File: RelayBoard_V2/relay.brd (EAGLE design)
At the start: 127 x 114.3 mm, 30 parts, among them K1 T9AS1D12-5, K2 T9AS1D12-5, T1 2N2222, T2 2N2222, T3 2N2222, T4 2N2222, X1 22-23-2021

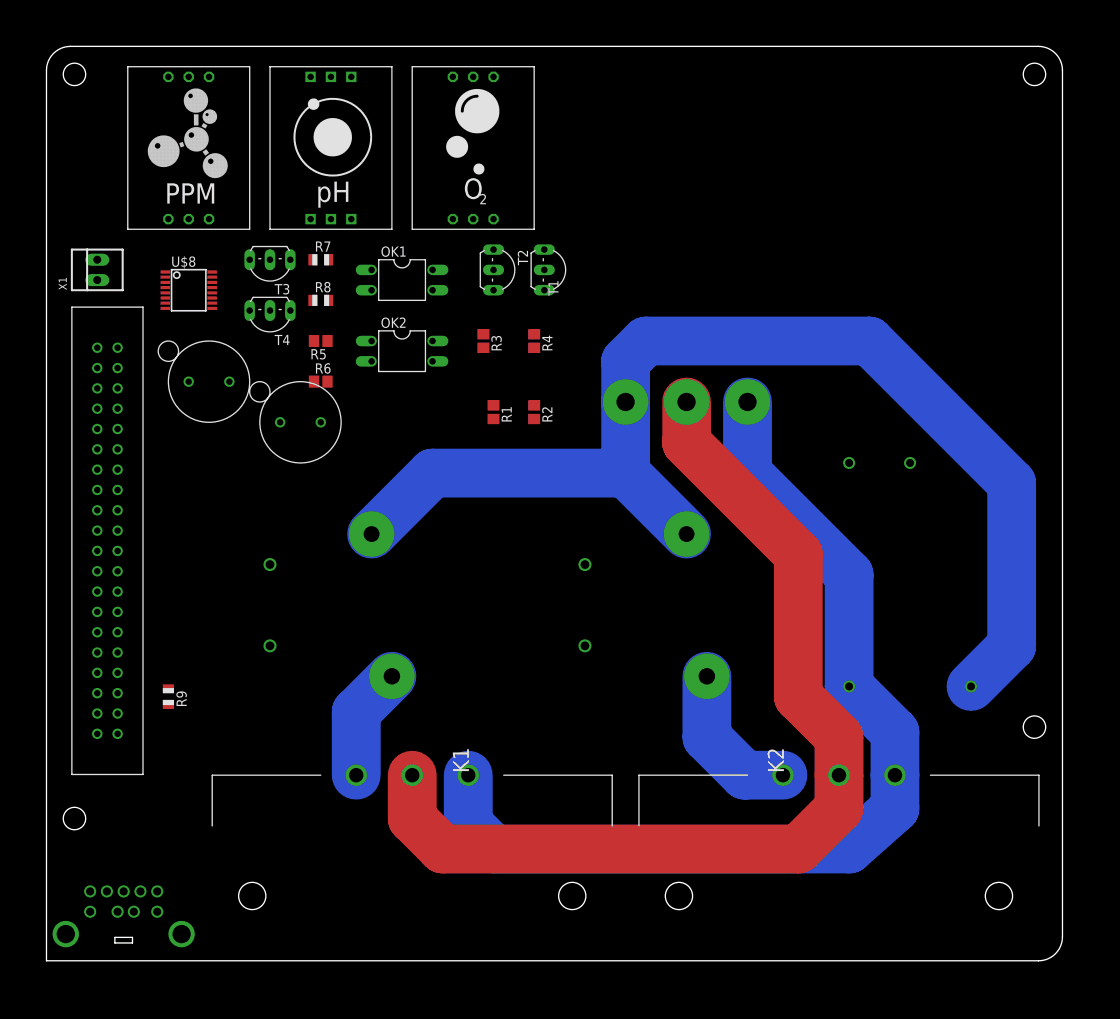
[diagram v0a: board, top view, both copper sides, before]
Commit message: Route everything. Add logo
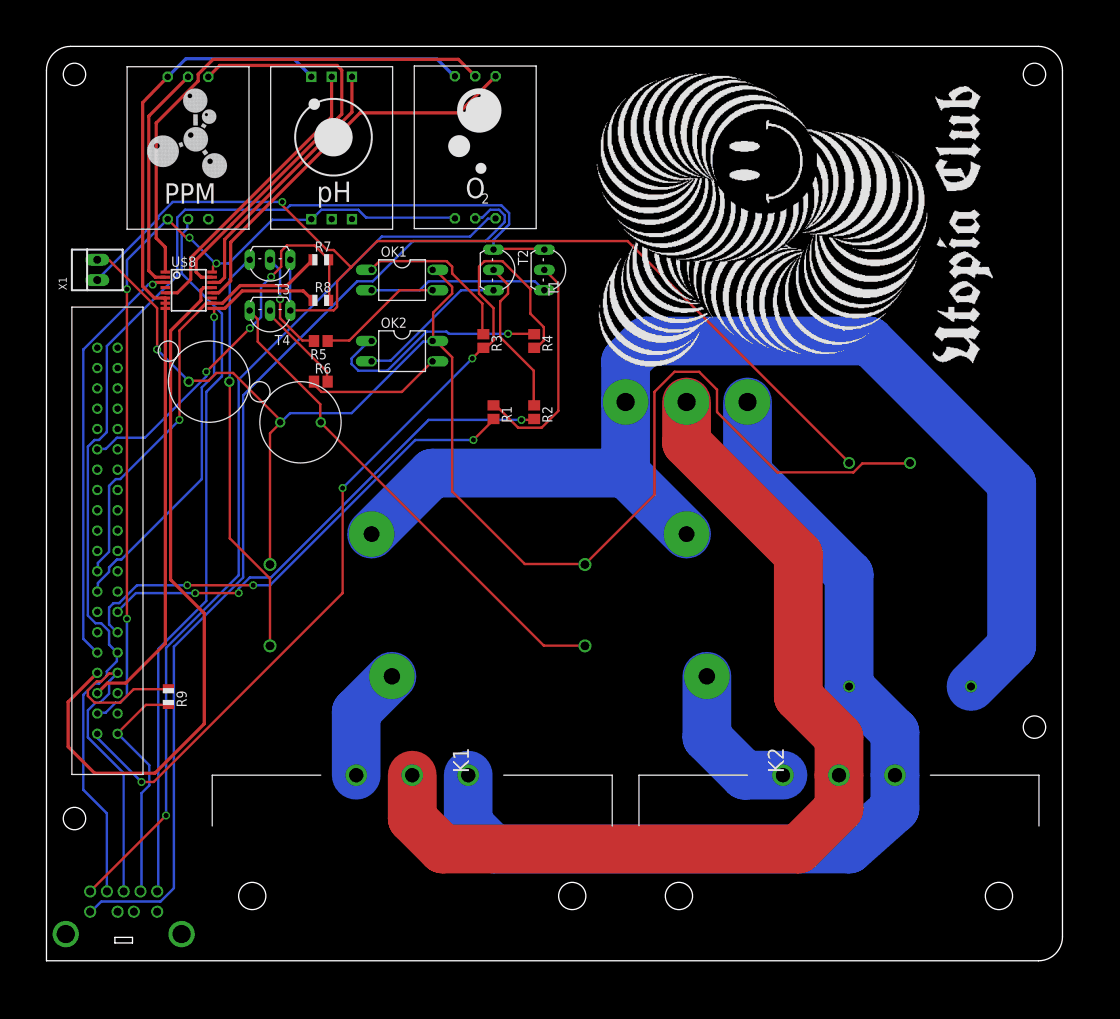
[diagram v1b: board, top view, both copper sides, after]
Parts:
- moved U$9 0.27 mm to (53.6, 101.7)
- moved U$10 0.08 mm to (35.6, 101.6)
- moved U$11 0.08 mm to (17.7, 101.6)
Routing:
- net N$32: track 0.00 -> 194.2 mm, vias 0 -> 1
- net DGND: track 0.00 -> 148.9 mm
- net AGND: track 0.00 -> 132.8 mm, vias 0 -> 1
- net N$30: track 0.00 -> 126.5 mm
- net N$41: track 0.00 -> 123.8 mm
- net N$31: track 0.00 -> 112.1 mm, vias 0 -> 1
- net N$6: track 0.00 -> 109.8 mm, vias 0 -> 3
- net N$33: track 0.00 -> 109.1 mm, vias 0 -> 4
- net N$7: track 0.00 -> 90.7 mm
- net N$37: track 0.00 -> 89.8 mm
- net N$26: track 0.00 -> 63.6 mm
- net N$1: track 0.00 -> 62.4 mm, vias 0 -> 3
- net N$16: track 0.00 -> 62.3 mm
- net N$2: track 0.00 -> 61.5 mm, vias 0 -> 3
- net N$28: track 0.00 -> 55.9 mm, vias 0 -> 1
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
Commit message: GND pour and add gerbers
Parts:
- renumbered U$8 to MUX
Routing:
- added copper zone on layer 1, net GND
- added copper zone on layer 16, net GND
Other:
- board text added: "jackbowen.github.io"

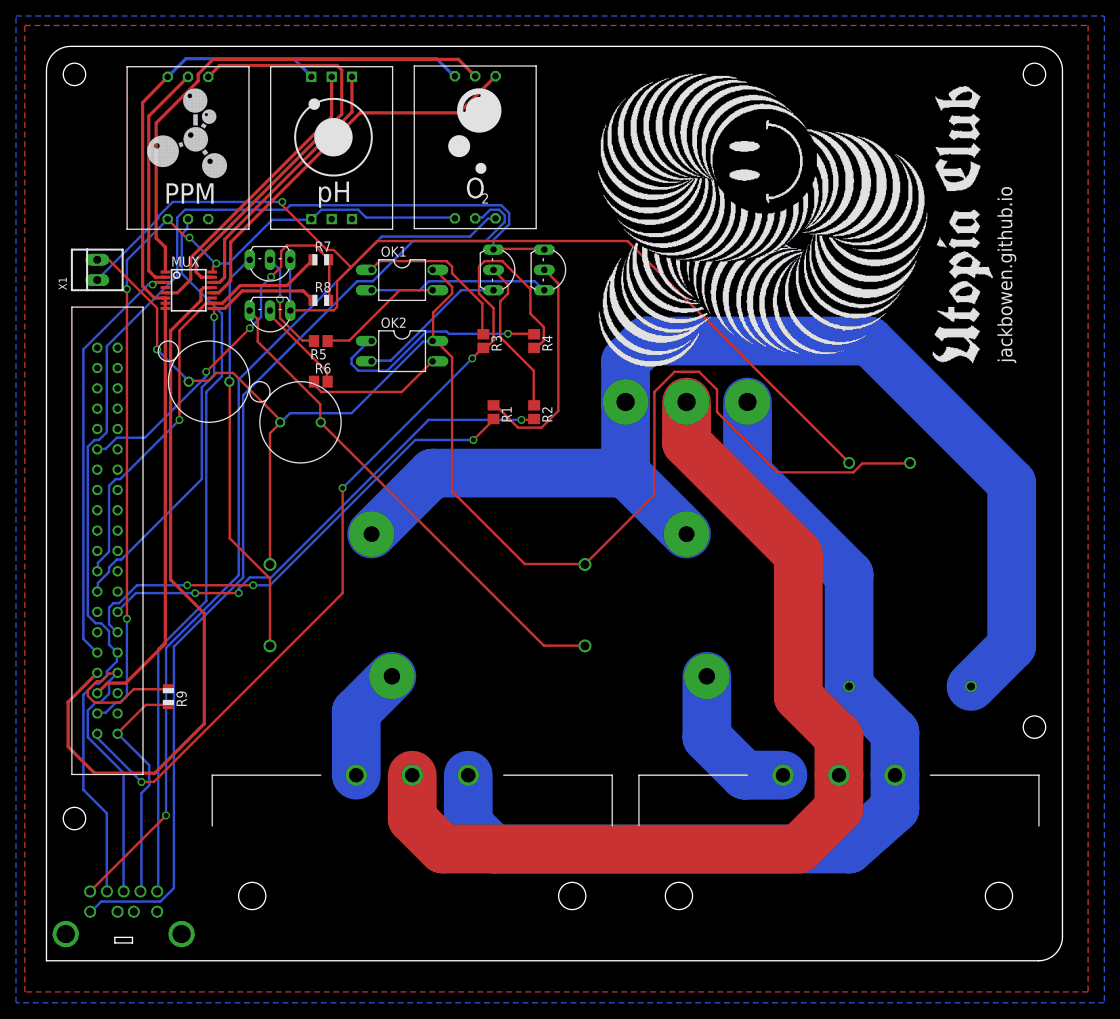
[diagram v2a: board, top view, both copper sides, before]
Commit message: Reduced DPI of silkscreen to OSH Park can actually fabricate them. New gerbers.
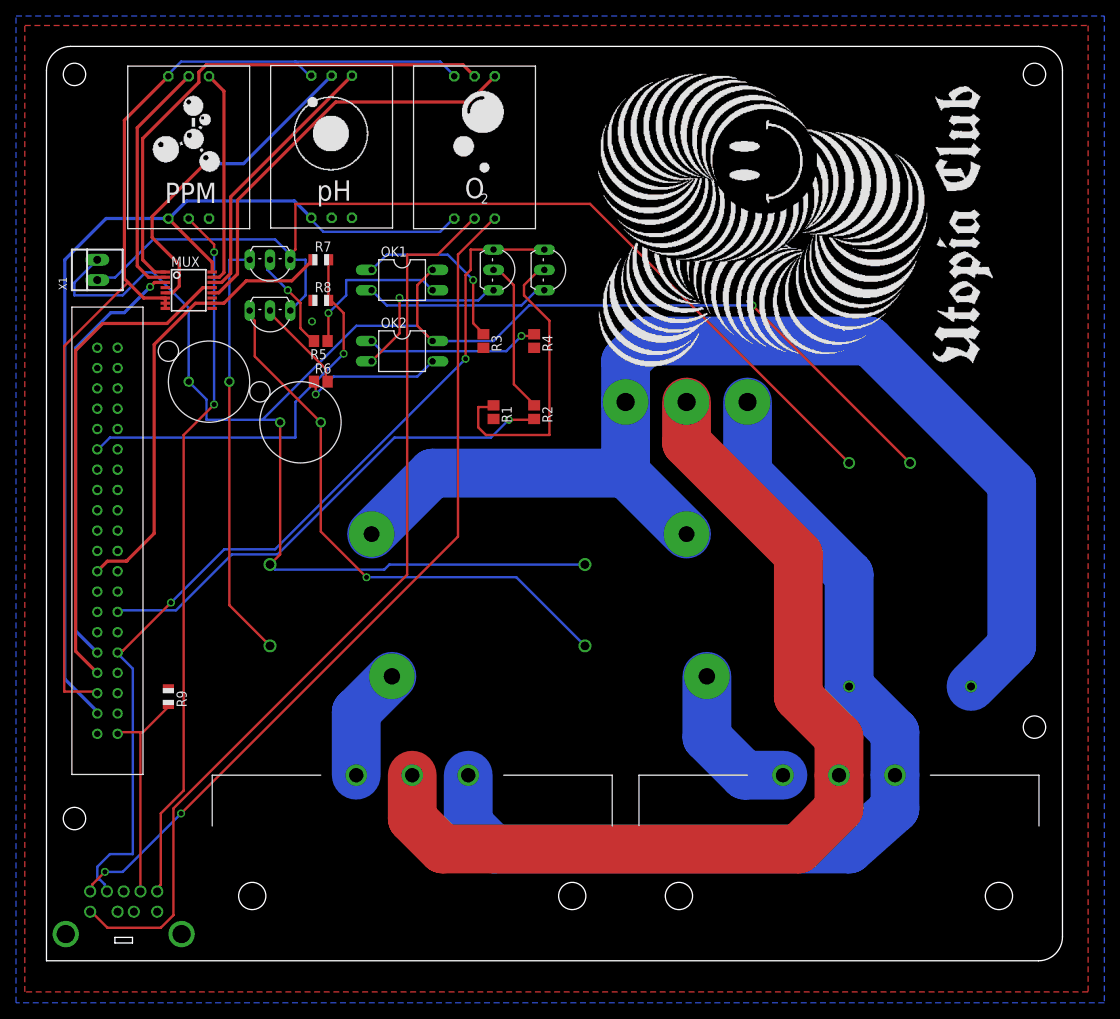
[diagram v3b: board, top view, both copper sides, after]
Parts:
- removed U$10: ATLAS_PH_WITH_ICON, BloomWall:ATLAS_PH_WITH_ICON
- removed U$11: ATLAS_PPM_WITH_ICON, BloomWall:ATLAS_PPM_WITH_ICON
- added U$5: ATLAS_DO_WITH_ICON, BloomWall:ATLAS_DO_WITH_ICON
- added U$8: ATLAS_PH_WITH_ICON, BloomWall:ATLAS_PH_WITH_ICON
- U$9: value ATLAS_DO_WITH_ICON -> ATLAS_PPM_WITH_ICON; device BloomWall:ATLAS_DO_WITH_ICON -> BloomWall:ATLAS_PPM_WITH_ICON
- moved U$9 35.8 mm to (17.8, 101.7)
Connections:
- removed net GND2: U$1.GND2
- removed net GND3: U$1.GND3
- removed net GND4: U$1.GND4
- removed net GND5: U$1.GND5
- removed net N$2: R1.2, U$1.GND1
- removed net N$28: MUX.B, R8.1, U$1.GND6
- removed net N$35: R9.1, U$1.GND, U$4.P5
- removed net N$6: R3.2, R4.2, U$1.GND7
- new net GND: MUX.B, R1.2, R3.2, R4.2, R8.1, R9.1, U$1.GND, U$1.GND1, U$1.GND2, U$1.GND3, U$1.GND4, U$1.GND5, U$1.GND6, U$1.GND7, U$4.P5
- net N$22: now also U$9.TX; no longer U$11.TX
- net N$23: now also U$9.RX; no longer U$11.RX
- net N$24: now also U$8.TX; no longer U$10.TX
- net N$25: now also U$8.RX; no longer U$10.RX
- net N$26: now also U$5.TX; no longer U$9.TX
- net N$27: now also U$5.RX; no longer U$9.RX
- net N$30: now also U$5.GND, U$8.GND; no longer U$10.GND, U$11.GND
- net N$31: now also U$5.PGND; no longer U$9.PGND
- net N$33: now also U$5.VCC, U$8.VCC; no longer U$10.VCC, U$11.VCC
- net N$37: now also U$9.PRB; no longer U$11.PRB
- net N$38: now also U$9.PRB2; no longer U$11.PRB2
- net N$39: now also U$8.PRB; no longer U$10.PRB
- net N$40: now also U$8.PGND; no longer U$10.PGND
- net N$41: now also U$5.PRB; no longer U$9.PRB
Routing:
- net N$6: track 109.8 -> 0.00 mm, vias 3 -> 0
- net N$2: track 61.5 -> 0.00 mm, vias 3 -> 0
- net N$28: track 55.9 -> 0.00 mm, vias 1 -> 0
- net N$35: track 47.5 -> 0.00 mm
- net DGND: track 148.9 -> 116.8 mm, vias 0 -> 2
- net N$7: track 90.7 -> 61.7 mm
- net N$23: track 52.5 -> 27.0 mm
- net N$32: track 194.2 -> 212.5 mm
- net N$33: track 109.1 -> 121.5 mm, vias 4 -> 0
- net N$3: track 28.6 -> 37.3 mm
- net N$16: track 62.3 -> 70.2 mm, vias 0 -> 1
- net N$30: track 126.5 -> 134.1 mm
- net N$10: track 29.4 -> 21.9 mm
- net N$41: track 123.8 -> 116.8 mm
- net AGND: track 132.8 -> 126.8 mm, vias 1 -> 0
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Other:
- board text removed: "jackbowen.github.io"

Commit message: decrease pad size for main connection
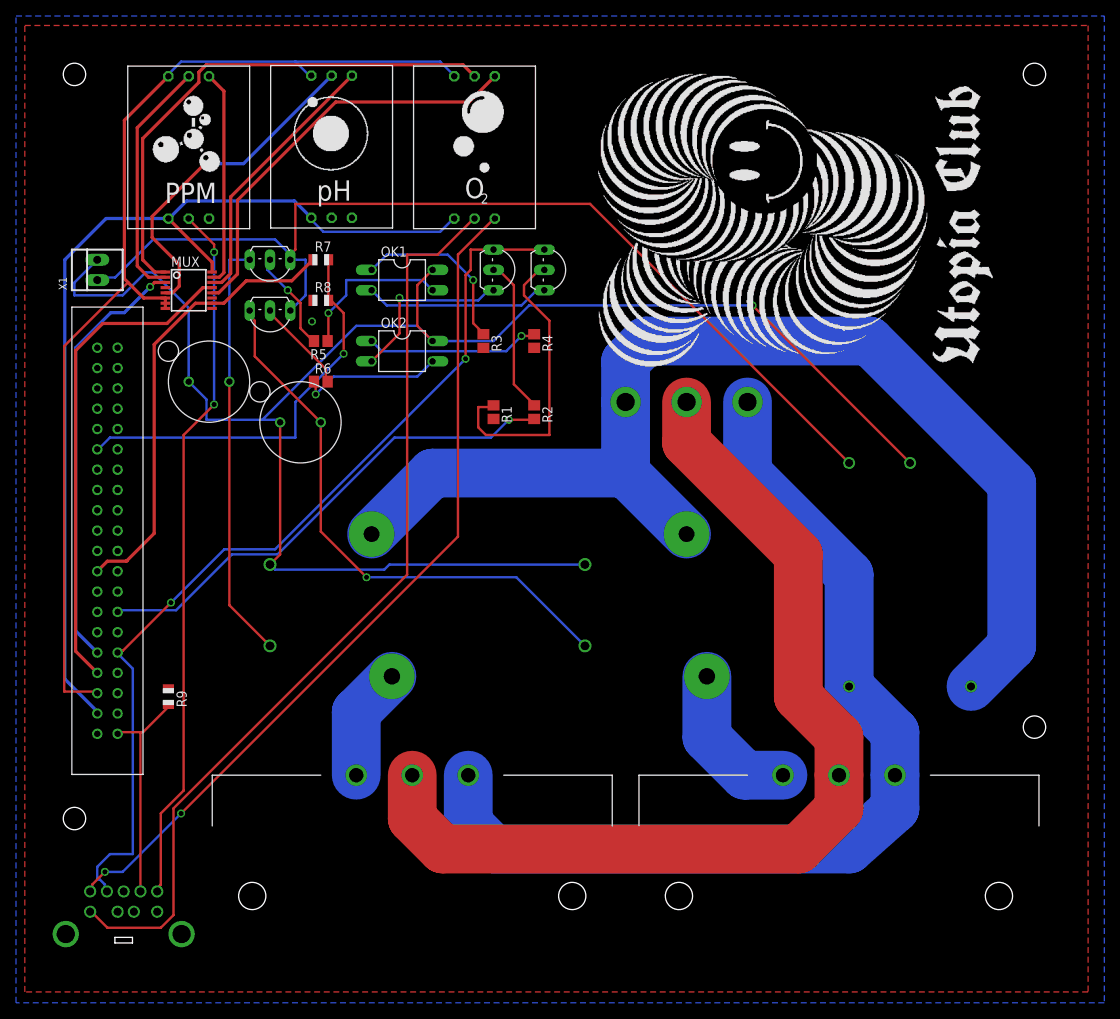
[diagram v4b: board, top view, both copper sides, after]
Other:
- board size 127 x 114.3 mm -> 2.2 x 0.7 mm
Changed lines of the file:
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@@
 <layers>
 <layer number="1" name="Top" color="4" fill="1" visible="yes" active="yes"/>
-<layer number="2" name="Route2" color="1" fill="3" visible="no" active="yes"/>
-<layer number="3" name="Route3" color="4" fill="3" visible="no" active="yes"/>
-<layer number="4" name="Route4" color="1" fill="4" visible="no" active="yes"/>
-<layer number="5" name="Route5" color="4" fill="4" visible="no" active="yes"/>
-<layer number="6" name="Route6" color="1" fill="8" visible="no" active="yes"/>
-<layer number="7" name="Route7" color="4" fill="8" visible="no" active="yes"/>
-<layer number="8" name="Route8" color="1" fill="2" visible="no" active="yes"/>
-<layer number="9" name="Route9" color="4" fill="2" visible="no" active="yes"/>
-<layer number="10" name="Route10" color="1" fill="7" visible="no" active="yes"/>
-<layer number="11" name="Route11" color="4" fill="7" visible="no" active="yes"/>
-<layer number="12" name="Route12" color="1" fill="5" visible="no" active="yes"/>
-<layer number="13" name="Route13" color="4" fill="5" visible="no" active="yes"/>
-<layer number="14" name="Route14" color="1" fill="6" visible="no" active="yes"/>
-<layer number="15" name="Route15" color="4" fill="6" visible="no" active="yes"/>
+<layer number="2" name="Route2" color="1" fill="3" visible="yes" active="yes"/>
+<layer number="3" name="Route3" color="4" fill="3" visible="yes" active="yes"/>
+<layer number="4" name="Route4" color="1" fill="4" visible="yes" active="yes"/>
+<layer number="5" name="Route5" color="4" fill="4" visible="yes" active="yes"/>
+<layer number="6" name="Route6" color="1" fill="8" visible="yes" active="yes"/>
+<layer number="7" name="Route7" color="4" fill="8" visible="yes" active="yes"/>
+<layer number="8" name="Route8" color="1" fill="2" visible="yes" active="yes"/>
+<layer number="9" name="Route9" color="4" fill="2" visible="yes" active="yes"/>
+<layer number="10" name="Route10" color="1" fill="7" visible="yes" active="yes"/>
+<layer number="11" name="Route11" color="4" fill="7" visible="yes" active="yes"/>
+<layer number="12" name="Route12" color="1" fill="5" visible="yes" active="yes"/>
+<layer number="13" name="Route13" color="4" fill="5" visible="yes" active="yes"/>
+<layer number="14" name="Route14" color="1" fill="6" visible="yes" active="yes"/>
+<layer number="15" name="Route15" color="4" fill="6" visible="yes" active="yes"/>
 <layer number="16" name="Bottom" color="1" fill="1" visible="yes" active="yes"/>
 <layer number="17" name="Pads" color="2" fill="1" visible="yes" active="yes"/>
@@
 <board>
 <plain>
-<wire x1="0" y1="0" x2="124.00000625" y2="0" width="0" layer="20"/>
-<wire x1="124.00000625" y1="0" x2="127" y2="2.99999375" width="0" layer="20" curve="90"/>
-<wire x1="127" y1="2.99999375" x2="127" y2="111.30000625" width="0" layer="20"/>
-<wire x1="127" y1="111.30000625" x2="124.00000625" y2="114.3" width="0" layer="20" curve="90"/>
-<wire x1="124.00000625" y1="114.3" x2="2.99999375" y2="114.3" width="0" layer="20"/>
-<wire x1="2.99999375" y1="114.3" x2="0" y2="111.30000625" width="0" layer="20" curve="90"/>
-<wire x1="0" y1="111.30000625" x2="0" y2="0" width="0" layer="20"/>
+<wire x1="0" y1="0" x2="124.00000625" y2="0" width="0" layer="249"/>
+<wire x1="124.00000625" y1="0" x2="127" y2="2.99999375" width="0" layer="249" curve="90"/>
+<wire x1="127" y1="2.99999375" x2="127" y2="111.30000625" width="0" layer="249"/>
+<wire x1="127" y1="111.30000625" x2="124.00000625" y2="114.3" width="0" layer="249" curve="90"/>
+<wire x1="124.00000625" y1="114.3" x2="2.99999375" y2="114.3" width="0" layer="249"/>
+<wire x1="2.99999375" y1="114.3" x2="0" y2="111.30000625" width="0" layer="249" curve="90"/>
+<wire x1="0" y1="111.30000625" x2="0" y2="0" width="0" layer="249"/>
 <hole x="3.49999375" y="110.80000625" drill="2.8"/>
 <hole x="123.50000625" y="110.80000625" drill="2.8"/>
